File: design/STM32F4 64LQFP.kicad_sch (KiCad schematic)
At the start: 15 parts, among them P2 SWD, U1 STM32F40X_LQFP64, X2 8MHz 10ppm

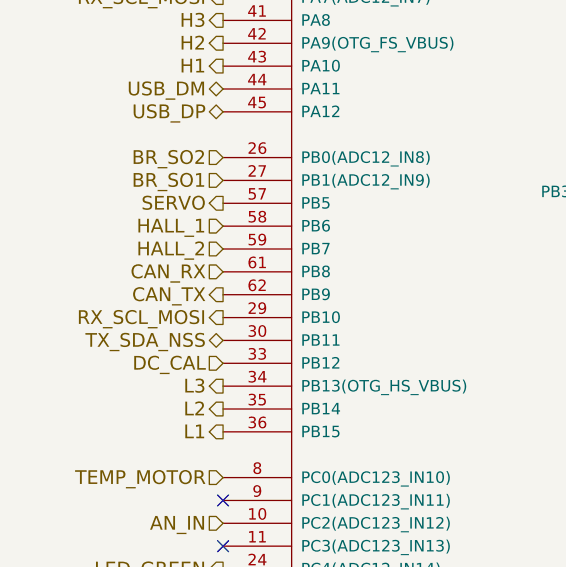
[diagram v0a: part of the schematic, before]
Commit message: Eliminado módulo CAN, agregado módulo bluetooth
Eliminado de hoja CAN, añadido de módulo bluetooth
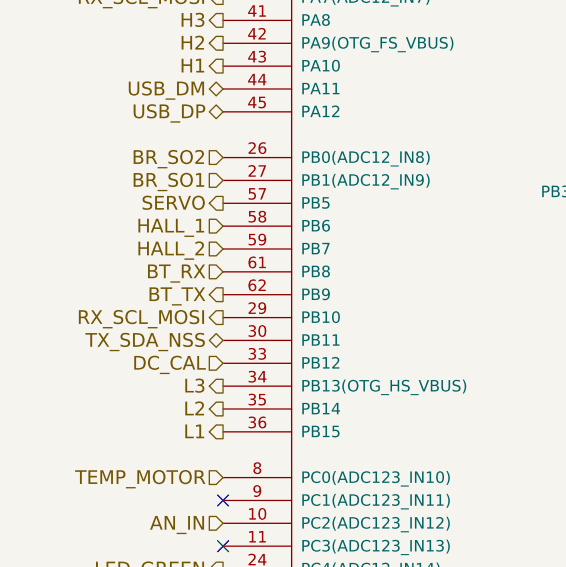
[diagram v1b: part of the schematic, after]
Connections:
- net CAN_RX renamed BT_RX
- net CAN_TX renamed BT_TX
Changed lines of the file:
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@@
 	)
 	(image
-		(at 44.45 170.18)
+		(at 46.99 161.29)
 		(data "iVBORw0KGgoAAAANSUhEUgAAAmoAAAJBCAIAAAB52w7dAAAAA3NCSVQICAjb4U/gAAAgAElEQVR4"
 			"nOydd1wTyf//JyGhExCkhiKoIDZEFPE4CxawYQOVoiLgiQ08VLAiip6K3oFYUQEVFPT0VBQLFrCh"
@@
 		)
 	)
-	(hierarchical_label "CAN_RX"
+	(hierarchical_label "BT_RX"
 		(shape input)
 		(at 114.3 92.71 180)
@@
 		)
 	)
-	(hierarchical_label "CAN_TX"
+	(hierarchical_label "BT_TX"
 		(shape output)
 		(at 114.3 95.25 180)
